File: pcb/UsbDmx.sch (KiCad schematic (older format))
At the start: 44 parts, among them CON101 10PIN_ISP_AVR, J101 USB_B, J102 Barrel_Jack, U101 74LS573, U102 USBN9604-28M, U103 AS6C6264, U104 L7805, U105 ATMEGA8515-16AU, U106 USBLC6-2SC6, Y101 24MHz

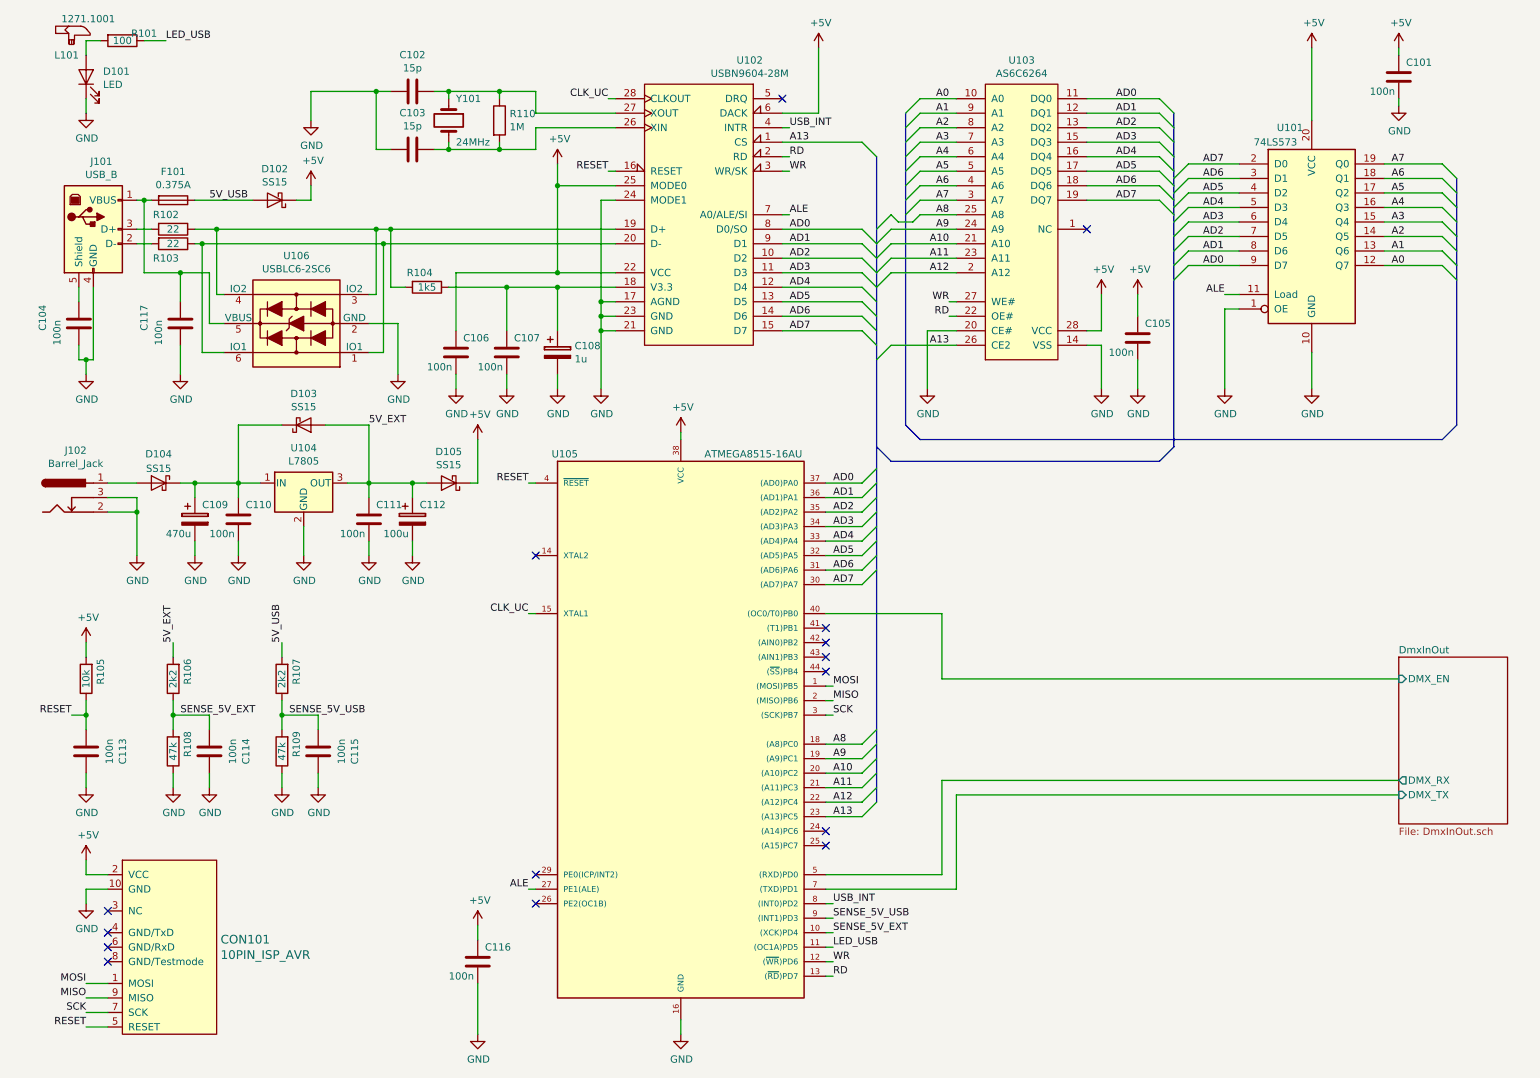
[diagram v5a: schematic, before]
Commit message: Bugfixing after testing prototype
Added a different pullup mechanism during programming to keep the USBN active during reset. Otherwise the ATmega loses its clock.
Fixed the broken pin association of the DMX connectors.
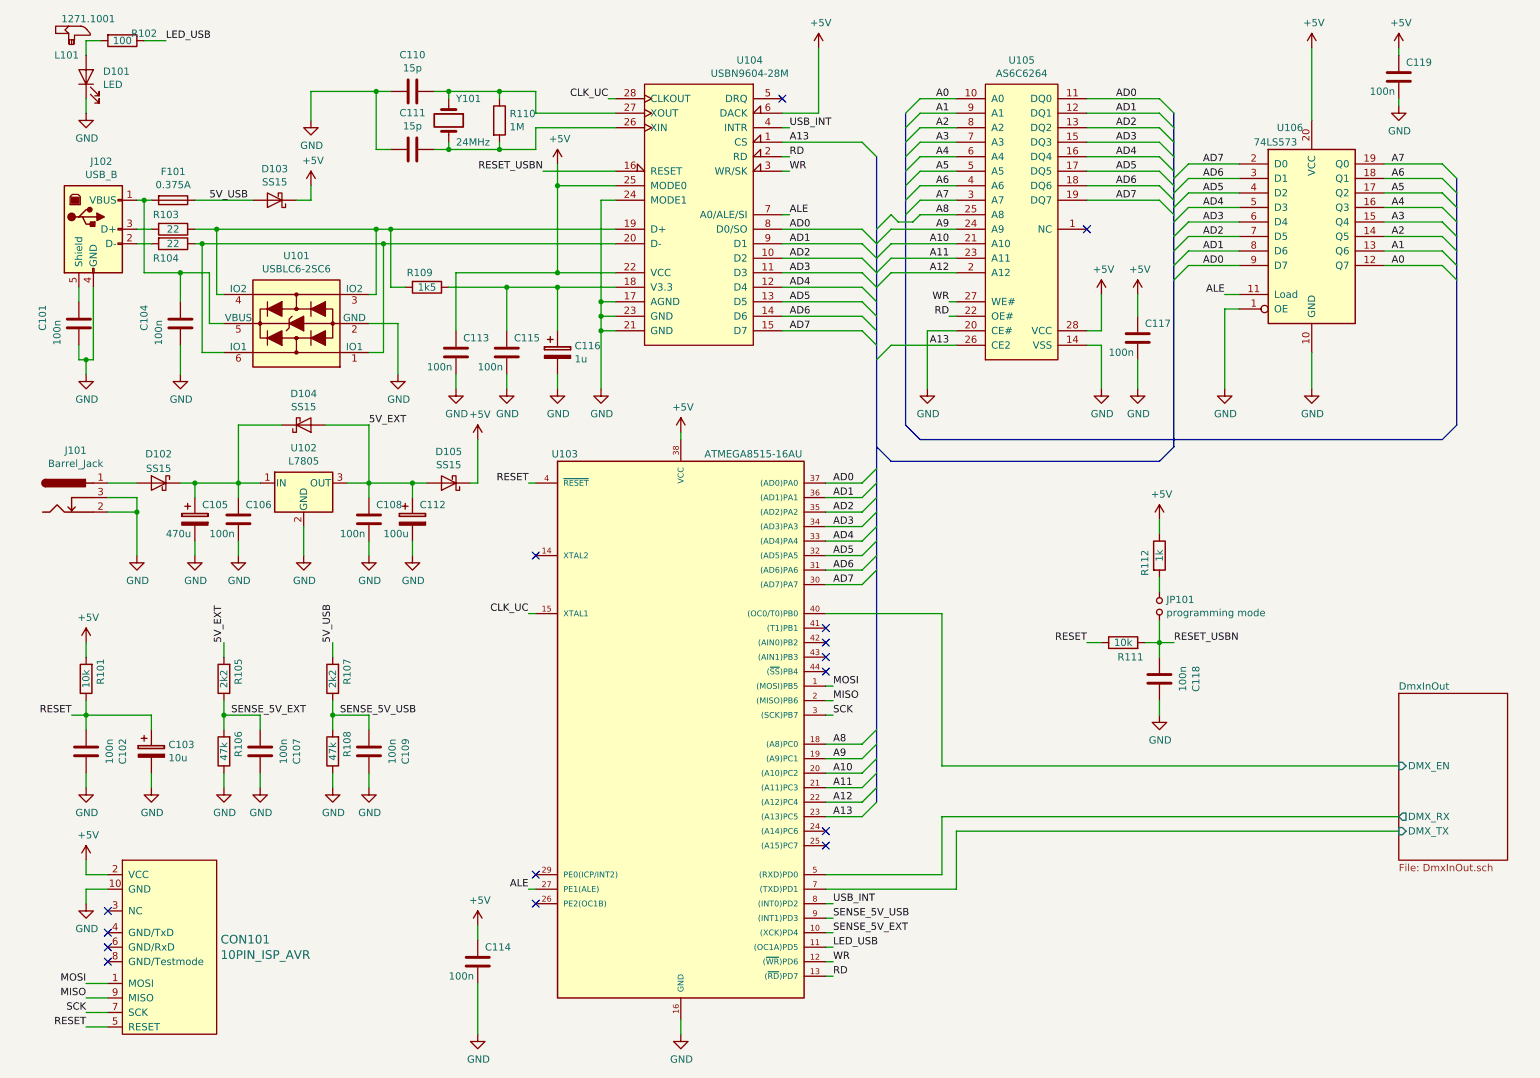
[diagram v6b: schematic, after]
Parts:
- added C103: 10u, Capacitors_THT:CP_Radial_D5.0mm_P2.00mm, symbol device:CP
- added C118: 100n, Capacitors_SMD:C_0603_HandSoldering, symbol device:C
- added JP101: programming mode, Pin_Headers:Pin_Header_Straight_1x02_Pitch2.54mm, symbol device:Jumper_NO_Small
- added R111: 10k, Resistors_SMD:R_0603_HandSoldering, symbol device:R
- added R112: 1k, Resistors_SMD:R_0603_HandSoldering, symbol device:R
- renumbered C104 to C101, C113 to C102, C117 to C104, C109 to C105, C110 to C106, C114 to C107, C111 to C108, C115 to C109, C102 to C110, C103 to C111, C106 to C113, C116 to C114, C107 to C115, C108 to C116, C105 to C117, C101 to C119, D104 to D102, D102 to D103, D103 to D104, J102 to J101, J101 to J102, R105 to R101, R101 to R102, R102 to R103, R103 to R104, R106 to R105, R108 to R106, R109 to R108, R104 to R109, U106 to U101, U104 to U102, U105 to U103, U102 to U104, U103 to U105, U101 to U106
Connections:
- net +5V: now also R112.1
- net GND: now also C103.2, C118.1
- net RESET: now also C103.1, R111.1; no longer U104.16 (RESET)
- new net: JP101.1, R112.2
- new net RESET_USBN: C118.2, JP101.2, R111.2, U104.16 (RESET)
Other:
- moved on the sheet: C107, C109, R105, R106, R107, R108

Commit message: fixed XLR connectors, LEDs and Reset
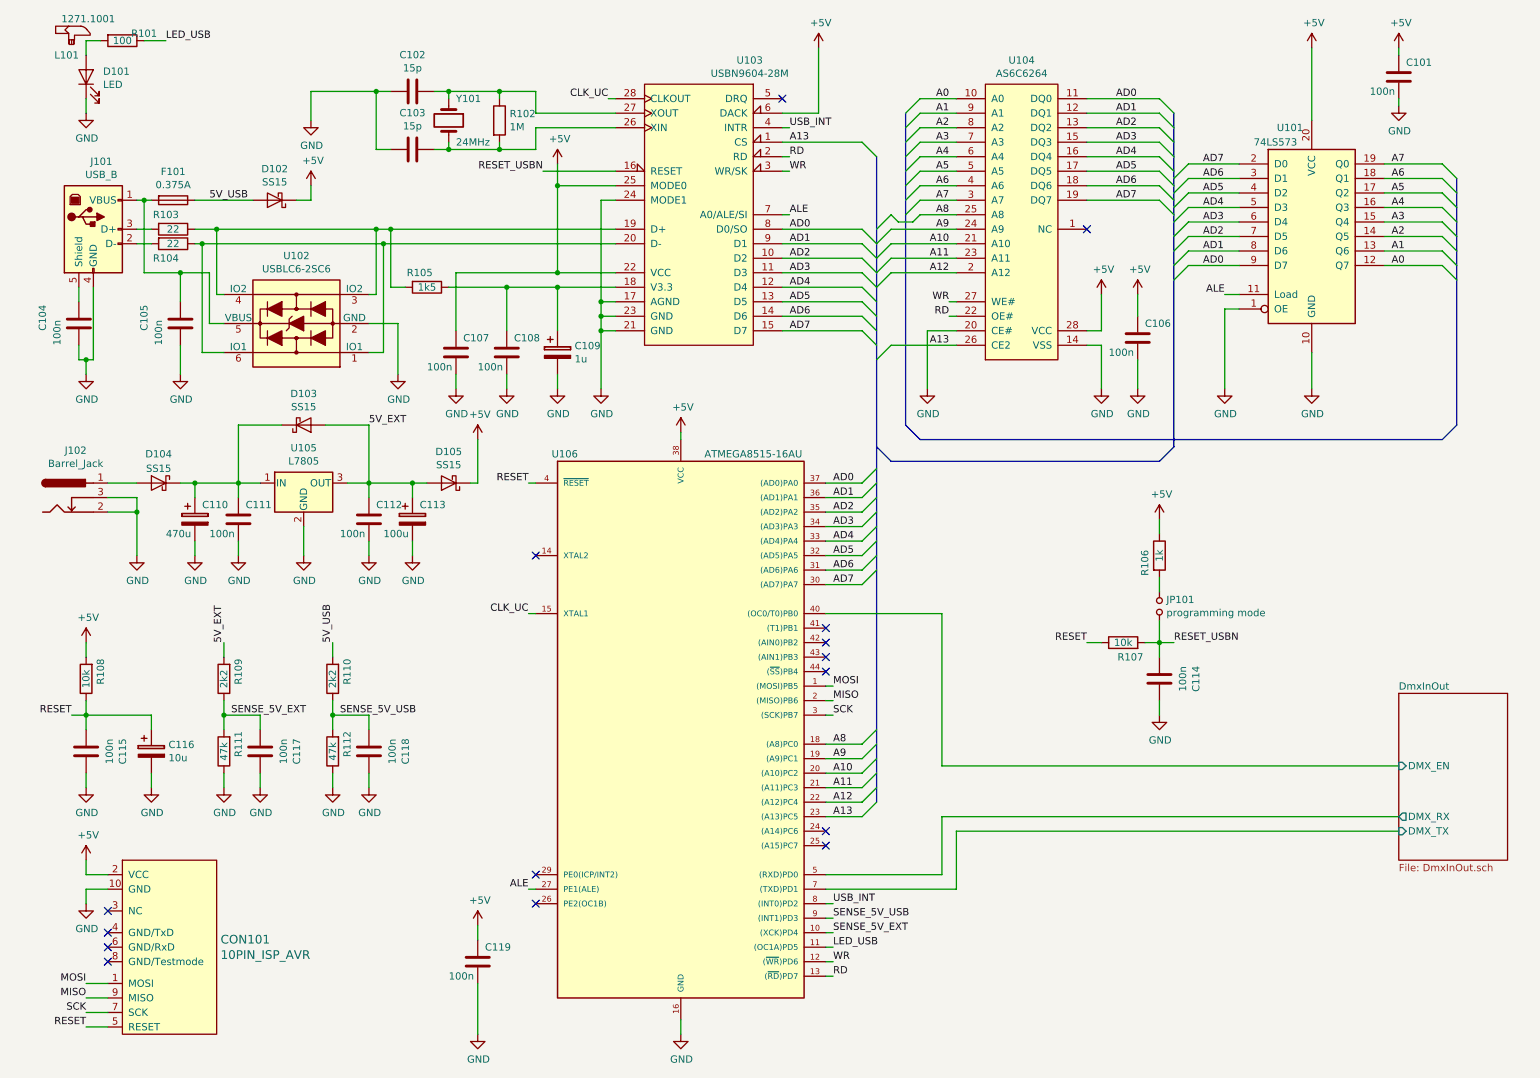
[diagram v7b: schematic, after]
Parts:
- renumbered C119 to C101, C110 to C102, C111 to C103, C101 to C104, C104 to C105, C117 to C106, C113 to C107, C115 to C108, C116 to C109, C105 to C110, C106 to C111, C108 to C112, C112 to C113, C118 to C114, C102 to C115, C103 to C116, C107 to C117, C109 to C118, C114 to C119, D103 to D102, D104 to D103, D102 to D104, J102 to J101, J101 to J102, R102 to R101, R110 to R102, R109 to R105, R112 to R106, R111 to R107, R101 to R108, R105 to R109, R107 to R110, R106 to R111, R108 to R112, U106 to U101, U101 to U102, U104 to U103, U105 to U104, U102 to U105, U103 to U106

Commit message: changed footprints to fit better the real parts
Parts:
- U104: footprint Housings_SOIC:SOIC-28W_7.5x17.9mm_Pitch1.27mm -> proz_soic:SOIC-28W_8.7x18.7mm_Pitch1.27mm
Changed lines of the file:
@@
 F 0 "U104" H 7350 4965 50  0000 C CNN
 F 1 "AS6C6264" H 7350 4874 50  0000 C CNN
-F 2 "Housings_SOIC:SOIC-28W_7.5x17.9mm_Pitch1.27mm" H 7100 2900 50  0001 C CNN
+F 2 "proz_soic:SOIC-28W_8.7x18.7mm_Pitch1.27mm" H 7100 2900 50  0001 C CNN
 F 3 "" H 7100 2900 50  0001 C CNN
 	1    7100 2900
